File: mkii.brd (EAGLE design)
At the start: 54 x 29 mm, 34 parts, among them IC1 AT90USB162-AU, IC2 GTL2003, Q1 16MHz, U5 TS1117, X1 MINI-USB-32005-301, X2 ISP, X3 PDI, X4 TPI

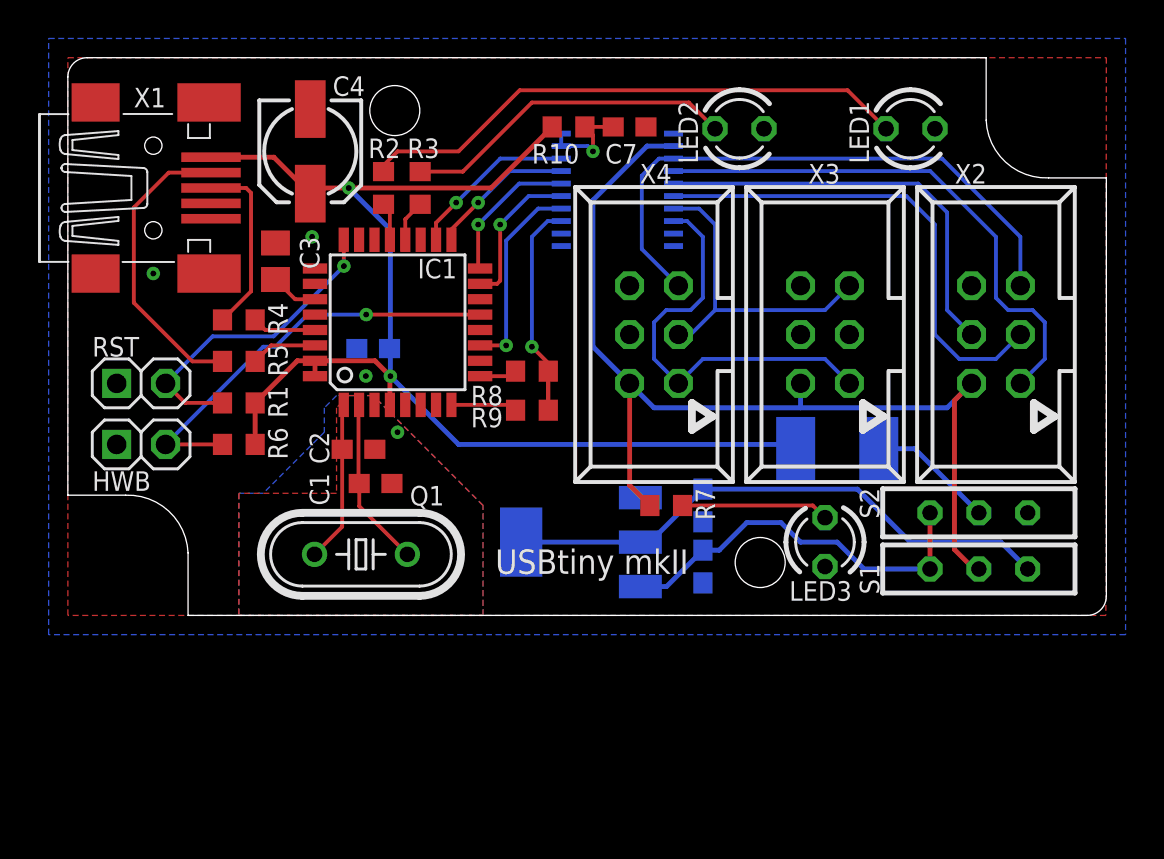
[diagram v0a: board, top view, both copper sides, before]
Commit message: changed led pins, rearranged everyting
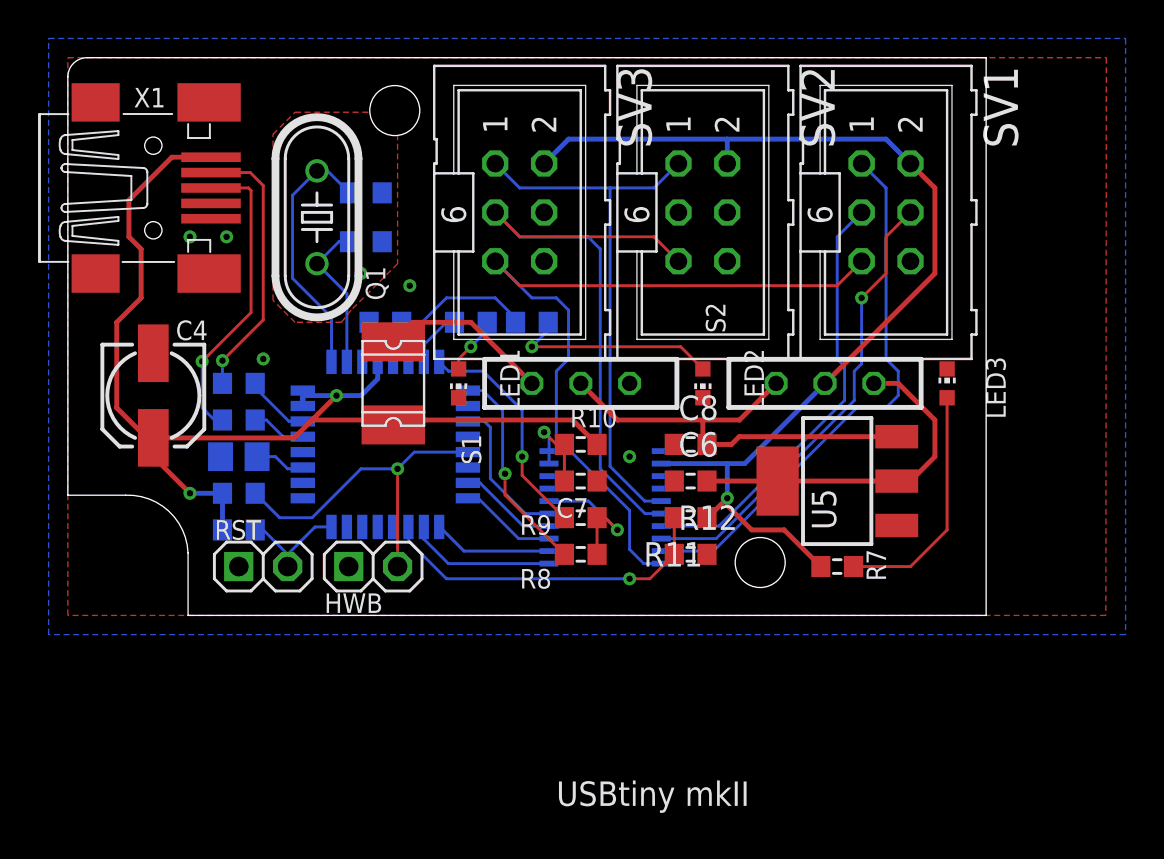
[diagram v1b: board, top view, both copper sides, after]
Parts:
- removed X2: ISP, con-panduit:057-006-1
- removed X3: PDI, con-panduit:057-006-1
- removed X4: TPI, con-panduit:057-006-1
- added R11, R12: 1M, rcl:R0603
- added SV1: ISP, con-ml:ML6
- added SV2: PDI, con-ml:ML6
- added SV3: TPI, con-ml:ML6
- IC1: value AT90USB162-AU -> ATMEGA32U4
- LED1, LED2, LED3: device led:LED3MM -> led:CHIP-LED0603
- R4, R5: value 27 -> 22
- S1, S2: value ESPESP101 -> ESPESP10XX; device schalter:ESP101 -> schalter:ESP10XX
- moved LED1 27.0 mm to (20.3, 12.1), turned to 180 degrees
- moved F1 23.3 mm to (16.9, 12.1), flipped to the top, turned to 90 degrees
- moved S1 21.8 mm to (26.7, 12.1)
- moved C7 18.6 mm to (26.7, 6.99)
- moved Q1 17.7 mm to (13.0, 20.7), turned to 270 degrees
- moved IC2 16.5 mm to (27.9, 5.62)
- moved R10 16.5 mm to (26.7, 8.89), turned to 180 degrees
- moved C4 15.1 mm to (4.45, 11.4)
- moved U5 13.7 mm to (40.0, 6.99), flipped to the top, turned to 90 degrees
- moved HWB 13.6 mm to (15.9, 2.54)
- moved LED2 13.4 mm to (33.0, 12.1), turned to 180 degrees
- moved C2 13.3 mm to (15.5, 22.0), flipped to the bottom, turned to 0 degrees
- moved C1 12.6 mm to (15.5, 19.4), flipped to the bottom, turned to 0 degrees
- moved S2 12.5 mm to (39.4, 12.1)
- moved RST 11.4 mm to (10.2, 2.54)
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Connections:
- removed net N$10: IC1.21, R2.2
- removed net N$22: F1.P$2, S1.C
- new net N$3: IC1.7, R2.2
- new net N$5: IC1.19, R11.2, R12.1
- new net N$6: F1.P$2, S1.2
- net GND: now also LED1.C, LED2.C, LED3.C, R12.2, SV1.6, SV2.6, SV3.6; no longer LED1.K, LED2.K, LED3.K, X2.6, X3.6, X4.6
- net N$11: now also IC1.6; no longer IC1.20
- net N$16: now also IC2.11; no longer IC2.18
- net N$17: now also IC2.12; no longer IC2.17
- net N$18: now also IC2.13; no longer IC2.16
- net N$19: now also IC2.14; no longer IC2.15
- net N$20: now also IC2.15; no longer IC2.14
- net N$21: now also IC2.16; no longer IC2.13
- net N$23: now also S1.C; no longer S1.2
- net N$25: now also IC2.5, SV2.1, SV3.1; no longer IC2.8, X3.1, X4.1
- net N$26: now also IC2.6, SV2.5, SV3.3; no longer IC2.7, X3.5, X4.3
- net N$27: now also IC2.10, SV1.5, SV3.5; no longer IC2.3, X2.5, X4.5
- net N$28: now also IC2.9, SV1.1; no longer IC2.4, X2.1
- net N$29: now also IC2.8, SV1.4; no longer IC2.5, X2.4
- net N$30: now also IC2.7, SV1.3; no longer IC2.6, X2.3
- net V+: now also R11.1, SV1.2, SV2.2, SV3.2; no longer X2.2, X3.2, X4.2
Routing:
- net N$12: track 28.9 -> 3.04 mm, vias 0 -> 1
- net N$5: track 0.00 -> 17.8 mm, vias 0 -> 1
- net N$26: track 16.9 -> 32.4 mm
- net N$32: track 29.9 -> 18.2 mm
- net !RST: track 16.6 -> 6.13 mm, vias 1 -> 0
- net N$27: track 30.8 -> 41.2 mm
- net N$9: track 1.95 -> 11.1 mm, vias 0 -> 1
- net N$6: track 0.00 -> 8.94 mm
- net N$31: track 3.45 -> 11.9 mm, vias 0 -> 1
- net N$25: track 21.8 -> 28.5 mm
- net N$22: track 6.59 -> 0.00 mm
- net N$1: track 9.40 -> 15.8 mm, vias 0 -> 1
- net N$13: track 17.4 -> 11.0 mm, vias 0 -> 1
- net N$11: track 2.16 -> 8.39 mm
- net N$21: track 13.3 -> 7.40 mm
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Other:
- board size 54 x 29 mm -> 47.8 x 29 mm

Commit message: align silk screen
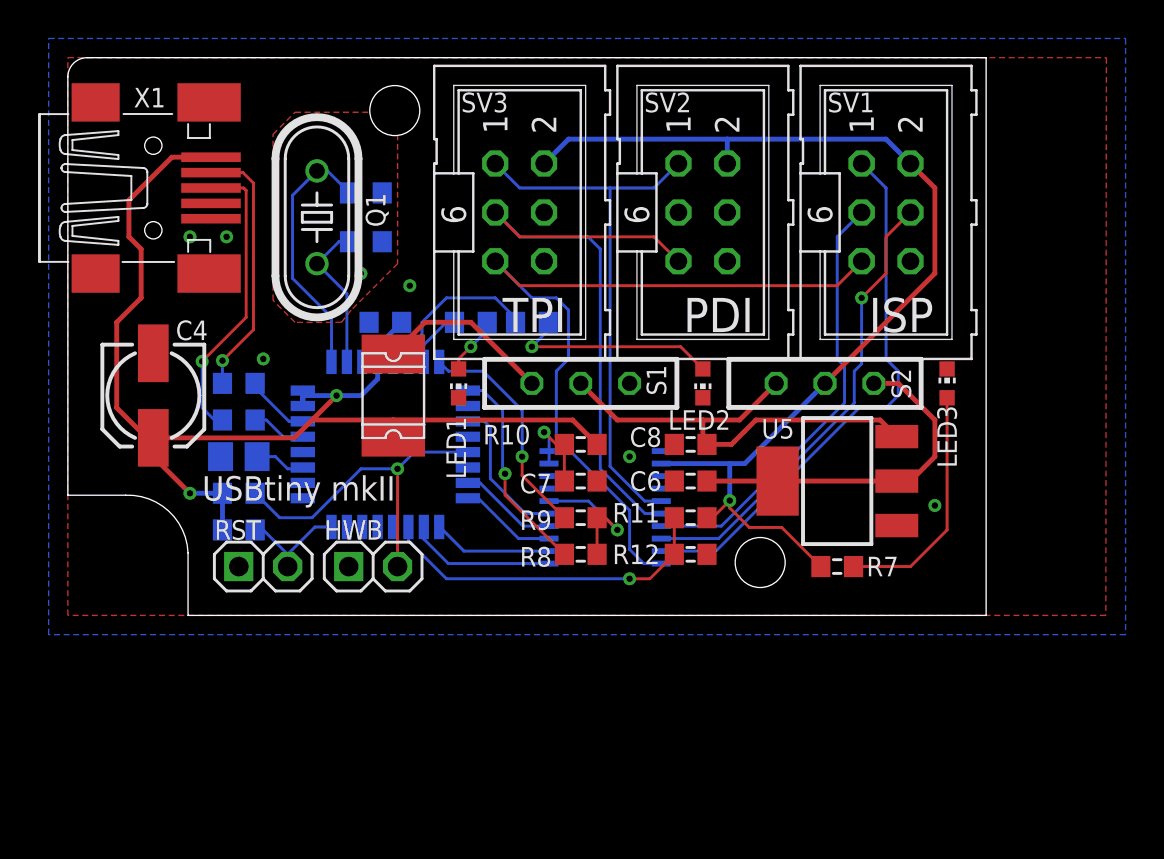
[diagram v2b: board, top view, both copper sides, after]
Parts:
- added U$1: CC-TPLACE-HALF, creative-commons:CC_TPLACE_HS
- added U$2: BY-TPLACE-HS, creative-commons:BY_TPLACE_HS
- added U$3: SA-TPLACE-HALF, creative-commons:SA_TPLACE_HS
- moved F1 0.63 mm to (16.9, 11.4)
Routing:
- net N$23: track 23.1 -> 23.9 mm
- net N$2: track 14.2 -> 13.5 mm
- net VCC: track 61.7 -> 62.3 mm

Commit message: sheep power
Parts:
- added U$4: SCHAF10MM, grafiken:SCHAF-10
- renumbered IC2 to U1, U5 to U2
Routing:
- net N$26: track 32.4 -> 27.0 mm, vias 0 -> 1
- net N$27: track 41.2 -> 37.6 mm, vias 0 -> 1
- net V+: track 55.8 -> 54.1 mm

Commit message: pacman arrived
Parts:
- added U$10, U$11, U$12, U$13, U$14, U$15, U$8, U$9: PM-DOT5, grafiken:PM-DOT5
- added U$16: PM-GHOSTA5, grafiken:PM-GHOSTA-5
- added U$5: PM-CHERRY5, grafiken:PM-CHERRY-5
- added U$6: PM-PILL5, grafiken:PM-PILL-5
- U$4: value SCHAF10MM -> SCHAF5MM; device grafiken:SCHAF-10 -> grafiken:SCHAF-5
- moved U$4 39.0 mm to (8.06, 9.21), flipped to the top
- moved U$3 0.14 mm to (40.3, 12.8)
- moved U$1 0.09 mm to (40.3, 23.1)
- moved U$2 0.09 mm to (40.3, 18.0)
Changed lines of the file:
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@@
 <layer number="201" name="201bmp" color="2" fill="1" visible="no" active="no"/>
 <layer number="202" name="202bmp" color="3" fill="1" visible="no" active="no"/>
+<layer number="203" name="203bmp" color="4" fill="10" visible="no" active="yes"/>
 <layer number="217" name="217bmp" color="18" fill="1" visible="no" active="no"/>
 <layer number="218" name="218bmp" color="19" fill="1" visible="no" active="no"/>
@@
 <hole x="17" y="26.25" drill="2.6"/>
 <hole x="36" y="2.75" drill="2.6"/>
-<text x="6.985" y="6.604" size="1.27" layer="21" align="center-left">USBtiny mkII</text>
+<text x="7.62" y="6.604" size="1.27" layer="21" align="center-left">USBtiny mkII</text>
 <wire x1="16.002" y1="16.764" x2="16.002" y2="15.367" width="0.254" layer="41"/>
 <wire x1="16.002" y1="15.367" x2="11.557" y2="15.367" width="0.254" layer="41"/>
@@
 <circle x="36" y="2.75" radius="1.25" width="1.5" layer="41"/>
 <circle x="17" y="26.25" radius="1.25" width="1.5" layer="41"/>
+<polygon width="0.25" layer="22">
+<vertex x="40.857621875" y="1.90433125" curve="-9.500037"/>
+<vertex x="40.452721875" y="2.11286875"/>
+<vertex x="39.447353125" y="1.29295625"/>
+<vertex x="38.75795625" y="1.982353125"/>
+<vertex x="39.57786875" y="2.987721875" curve="-19.000015"/>
+<vertex x="39.23048125" y="3.826384375"/>
+<vertex x="37.939815625" y="3.957521875"/>
+<vertex x="37.939815625" y="4.932478125"/>
+<vertex x="39.23048125" y="5.063615625" curve="-19.000015"/>
+<vertex x="39.57786875" y="5.902278125"/>
+<vertex x="38.75795625" y="6.907646875"/>
+<vertex x="39.447353125" y="7.59704375"/>
+<vertex x="40.452721875" y="6.77713125" curve="-19.000015"/>
+<vertex x="41.291384375" y="7.12451875"/>
+<vertex x="41.422521875" y="8.415184375"/>
+<vertex x="42.397478125" y="8.415184375"/>
+<vertex x="42.528615625" y="7.12451875" curve="-19.000015"/>
+<vertex x="43.367278125" y="6.77713125"/>
+<vertex x="44.372646875" y="7.59704375"/>
+<vertex x="45.06204375" y="6.907646875"/>
+<vertex x="44.24213125" y="5.902278125" curve="-19.000015"/>
+<vertex x="44.58951875" y="5.063615625"/>
+<vertex x="45.880184375" y="4.932478125"/>
+<vertex x="45.880184375" y="3.957521875"/>
+<vertex x="44.58951875" y="3.826384375" curve="-19.000015"/>
+<vertex x="44.24213125" y="2.987721875"/>
+<vertex x="45.06204375" y="1.982353125"/>
+<vertex x="44.372646875" y="1.29295625"/>
+<vertex x="43.367278125" y="2.11286875" curve="-9.500037"/>
+<vertex x="42.962378125" y="1.90433125"/>
+<vertex x="42.388353125" y="3.29015" curve="67.500062"/>
+<vertex x="43.16" y="4.445" curve="247.50006"/>
+<vertex x="41.431646875" y="3.29015"/>
+</polygon>
 </plain>
 <attributes>
@@
 <attribute name="VALUE" x="31.75" y="0.635" size="1.27" layer="27"/>
 </element>
-<element name="U$1" library="creative-commons" package="CC_TPLACE_HS" value="CC-TPLACE-HALF" x="40.259" y="23.114" rot="MR0"/>
-<element name="U$2" library="creative-commons" package="BY_TPLACE_HS" value="BY-TPLACE-HS" x="40.259" y="18.034" rot="MR0"/>
-<element name="U$3" library="creative-commons" package="SA_TPLACE_HS" value="SA-TPLACE-HALF" x="40.259" y="12.954" rot="MR0"/>
-<element name="U$4" library="grafiken" package="SCHAF-10" value="SCHAF10MM" x="46.355" y="1.905" rot="MR0"/>
+<element name="U$1" library="creative-commons" package="CC_TPLACE_HS" value="CC-TPLACE-HALF" x="40.3225" y="23.0505" rot="MR0"/>
+<element name="U$2" library="creative-commons" package="BY_TPLACE_HS" value="BY-TPLACE-HS" x="40.3225" y="17.9705" rot="MR0"/>
+<element name="U$3" library="creative-commons" package="SA_TPLACE_HS" value="SA-TPLACE-HALF" x="40.3225" y="12.827" rot="MR0"/>
+<element name="U$4" library="grafiken" package="SCHAF-5" value="SCHAF5MM" x="8.0645" y="9.2075"/>
+<element name="U$5" library="grafiken" package="PM-CHERRY-5" value="PM-CHERRY5" x="6.35" y="13.335" rot="MR0"/>
+<element name="U$6" library="grafiken" package="PM-PILL-5" value="PM-PILL5" x="11.43" y="23.495" rot="MR0"/>
+<element name="U$8" library="grafiken" package="PM-DOT5" value="PM-DOT5" x="6.35" y="8.255" rot="MR0"/>
+<element name="U$9" library="grafiken" package="PM-DOT5" value="PM-DOT5" x="16.51" y="23.495" rot="MR0"/>
+<element name="U$10" library="grafiken" package="PM-DOT5" value="PM-DOT5" x="21.59" y="23.495" rot="MR0"/>
+<element name="U$11" library="grafiken" package="PM-DOT5" value="PM-DOT5" x="6.35" y="23.495" rot="MR0"/>
+<element name="U$12" library="grafiken" package="PM-DOT5" value="PM-DOT5" x="26.67" y="23.495" rot="MR0"/>
+<element name="U$13" library="grafiken" package="PM-DOT5" value="PM-DOT5" x="6.35" y="18.415" rot="MR0"/>
+<element name="U$14" library="grafiken" package="PM-DOT5" value="PM-DOT5" x="31.75" y="18.415" rot="MR0"/>
+<element name="U$15" library="grafiken" package="PM-DOT5" value="PM-DOT5" x="31.75" y="23.495" rot="MR0"/>
+<element name="U$16" library="grafiken" package="PM-GHOSTA-5" value="PM-GHOSTA5" x="31.75" y="13.335" rot="MR0"/>
 </elements>
 <signals>

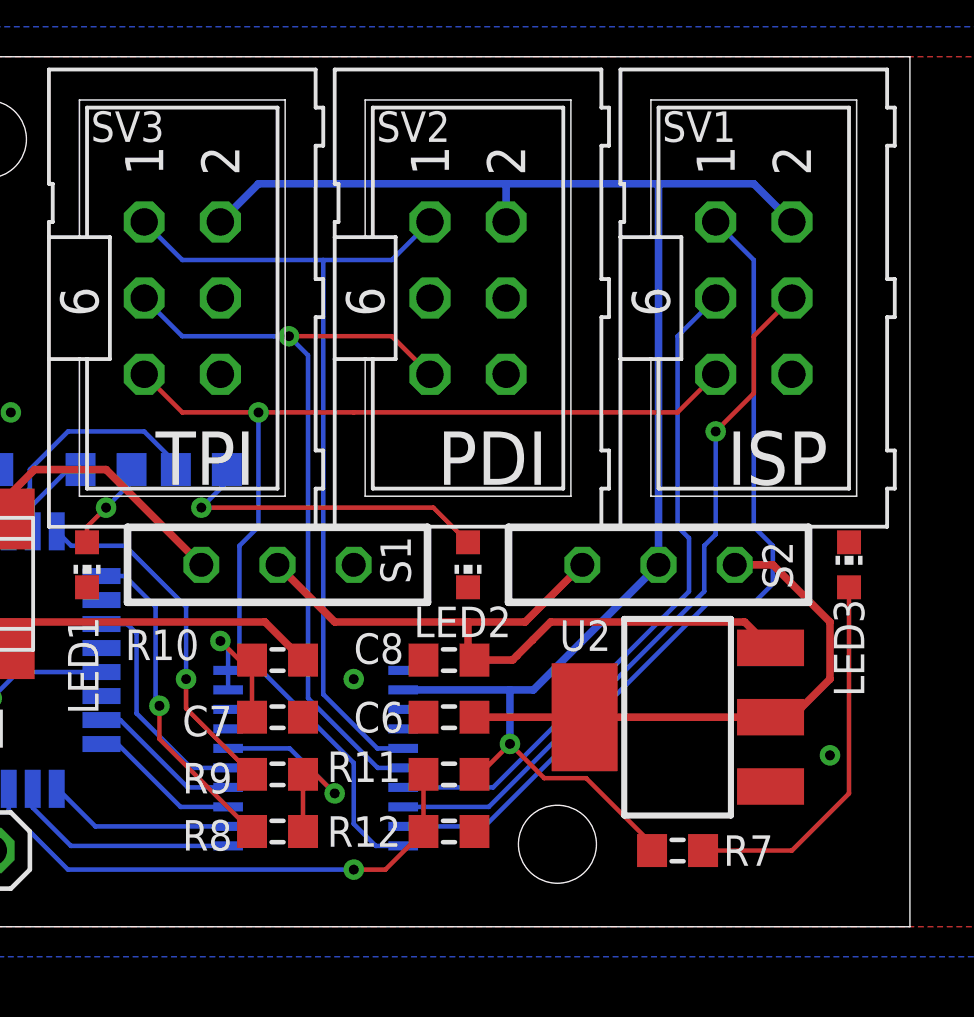
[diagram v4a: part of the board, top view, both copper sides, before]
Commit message: more gnd plane between data lines
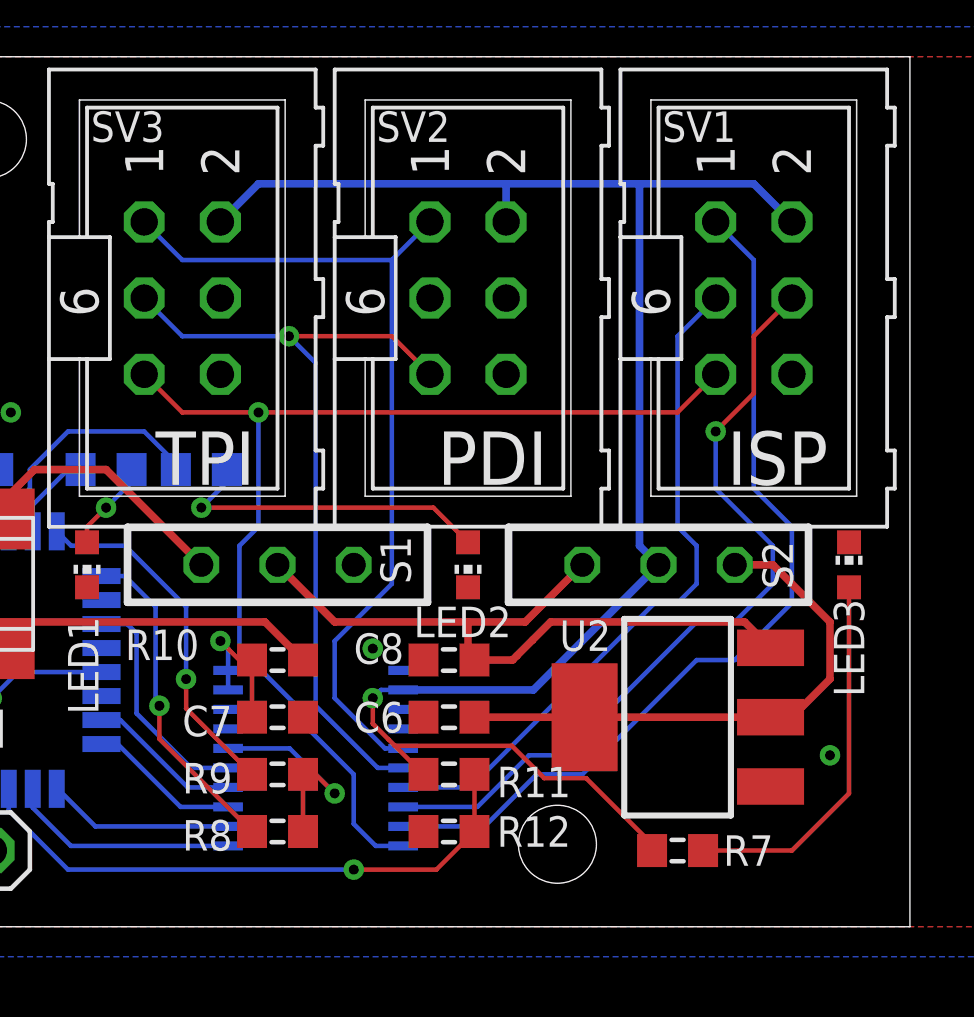
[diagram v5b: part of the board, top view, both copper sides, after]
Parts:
- turned R11 to 0 degrees
- turned R12 to 180 degrees
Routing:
- net V+: track 54.1 -> 59.1 mm
- net N$29: track 24.0 -> 26.8 mm
- net N$5: track 17.8 -> 19.5 mm
- net N$28: track 28.5 -> 29.8 mm
